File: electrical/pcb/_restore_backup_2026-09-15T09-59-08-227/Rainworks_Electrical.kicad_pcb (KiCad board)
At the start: 2 copper layers, 111.4 x 40.9 mm, 19 parts, among them J1 472192001, P1 ESP8266 Thing, U1 MCP3008, U10 S1_SM, U11 S0_PH, U7 S4_FR, U8 S3_T, U9 S2_C

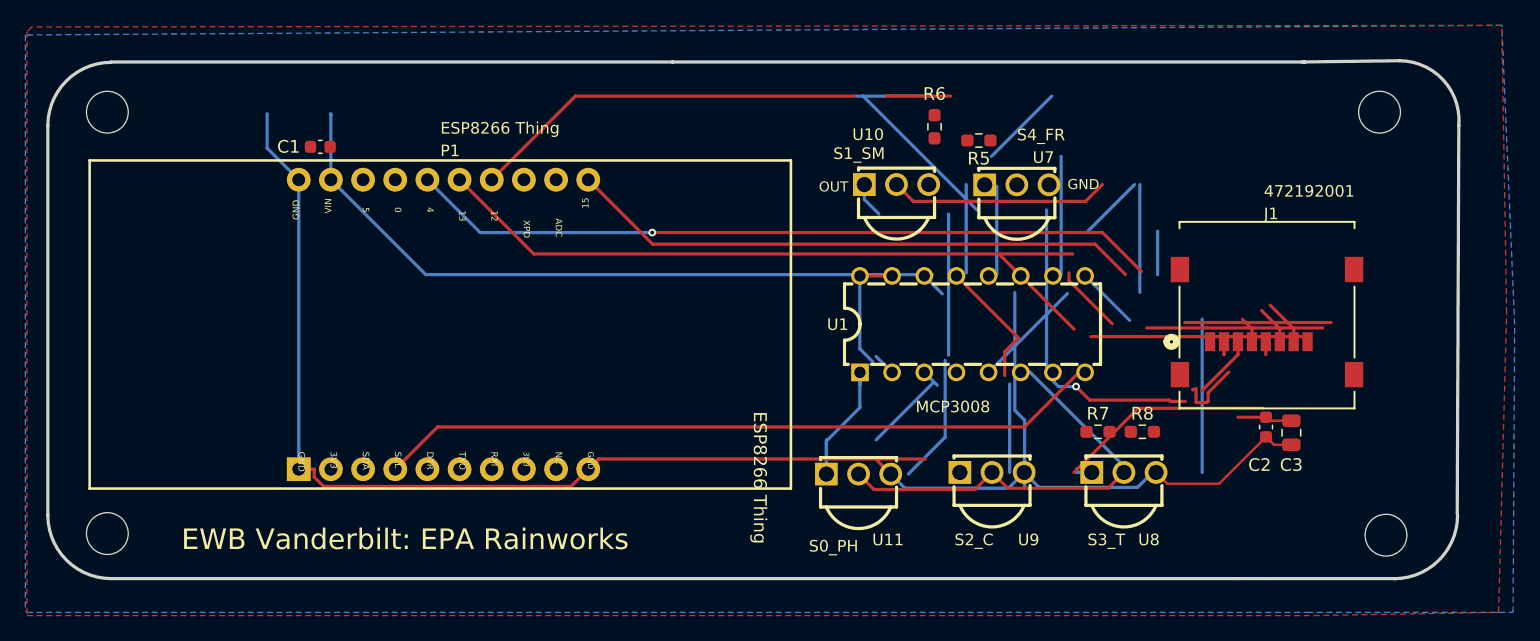
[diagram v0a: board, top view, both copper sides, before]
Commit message: Adding SD card passives and preparing for autorouter outside of KiCad, includes placement and schematic ERC checks
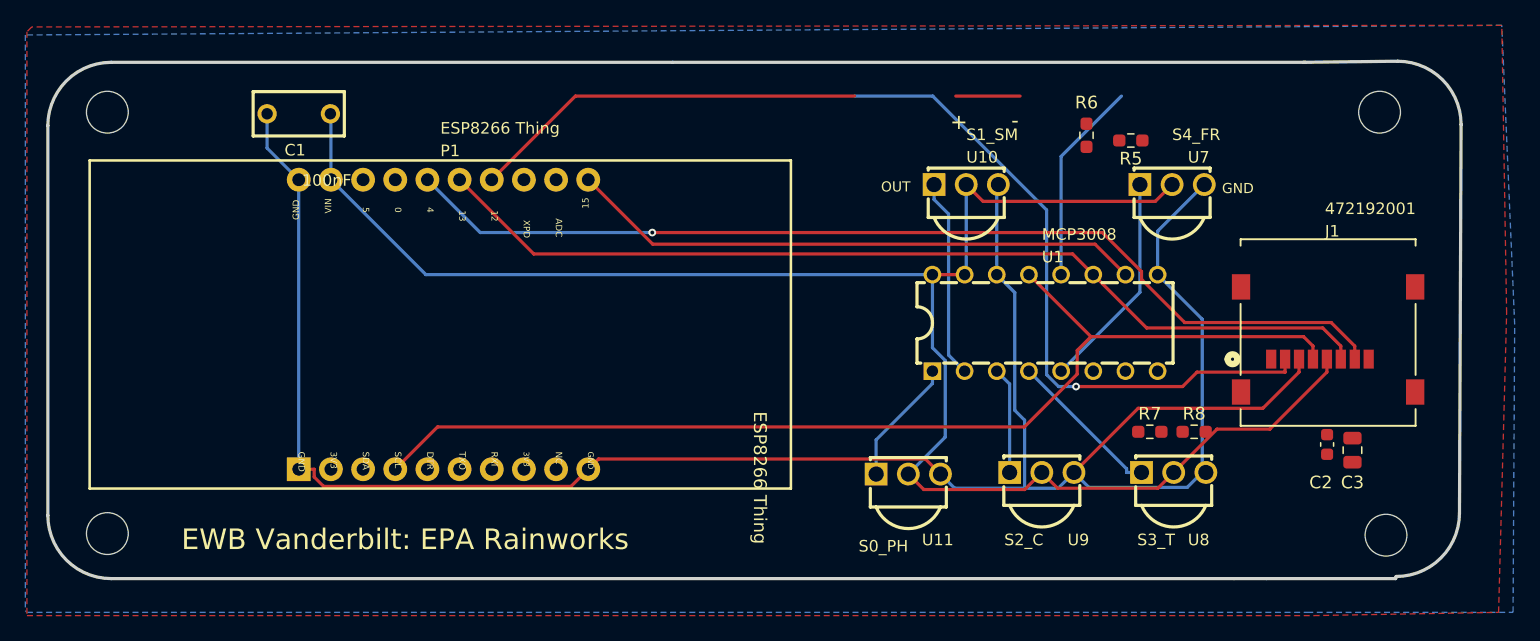
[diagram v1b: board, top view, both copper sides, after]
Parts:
- C1: footprint Capacitor_SMD:C_0603_1608Metric -> CAP-TH_L7.2-W3.5-P5.00-D0.5
- moved U7 12.3 mm to (185.8, 91.0)
- moved R6 12.0 mm to (179.0, 87.1)
- moved R5 12.0 mm to (182.5, 87.5)
- moved U1 5.73 mm to (175.7, 101.9)
- moved U10 5.50 mm to (169.5, 91.0)
- moved C2 5.02 mm to (198.0, 111.5)
- moved C3 5.02 mm to (200.0, 112.0)
- moved J1 5.02 mm to (198.1, 102.7)
- moved R7 4.09 mm to (184.0, 110.5)
- moved R8 4.09 mm to (187.5, 110.5)
- moved U11 3.93 mm to (164.9, 113.8)
- moved U9 3.93 mm to (175.5, 113.7)
- moved U8 3.93 mm to (185.9, 113.7)
- moved C1 3.12 mm to (116.8, 85.4)
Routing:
- net (no net): track 105.0 -> 169.4 mm
- net /SD_SCLK_SPI: track 123.2 -> 86.2 mm
- net /3V3_VDD: track 33.1 -> 0.00 mm
- net /SD_MISO_SPI: track 85.4 -> 100.1 mm
- net GND: track 192.1 -> 177.7 mm
- net /CH1_ADC: track 4.59 -> 15.7 mm
- net /CH4_ADC: track 8.80 -> 0.00 mm
- net /CH2_ADC: track 14.7 -> 8.42 mm
- net D1_2: track 0.00 -> 5.08 mm
- net /CH0_ADC: track 11.8 -> 9.97 mm
- net /S3_T_VOUT: track 1.47 -> 0.00 mm
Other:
- board size 111.4 x 40.9 mm -> 111.6 x 40.9 mm
- board text added: "+"
- board text added: "-"
